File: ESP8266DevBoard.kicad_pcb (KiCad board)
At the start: 2 copper layers, 105 x 60 mm, 60 parts, among them J1 10118192-0001LF, J2 RJ11-CHINA, J3 RJ11-CHINA, J4 AC, Q1 BC847BLT1G, Q2 BC847BLT1G, Q3 2N7002H6327XTSA2, Q4 2N7002H6327XTSA2, Q5 2N7002H6327XTSA2, Q6 2N7002H6327XTSA2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

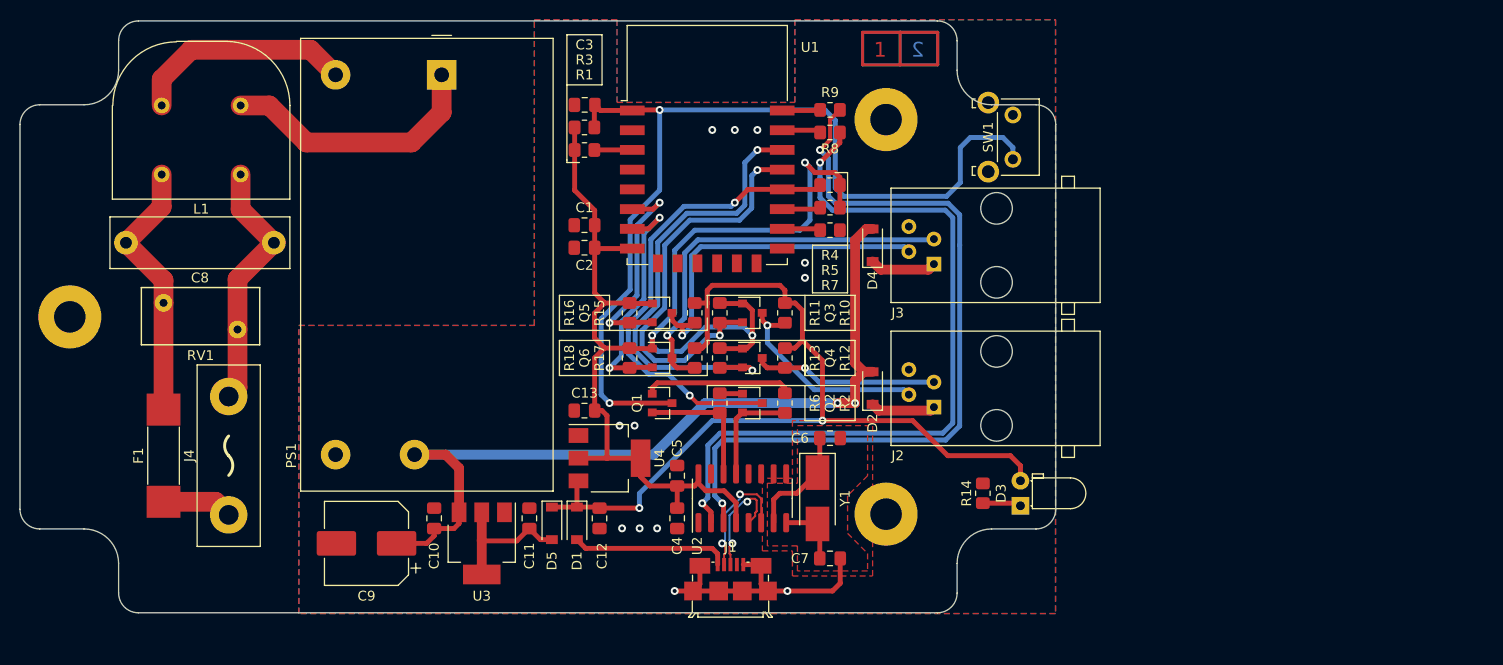
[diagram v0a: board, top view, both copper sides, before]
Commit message: RJ connectors changed, LED and buzzer controll lines added for each conector, readme file with rev changes added.
Signed-off-by: Ion Bold <bold.ion86@gmail.com>
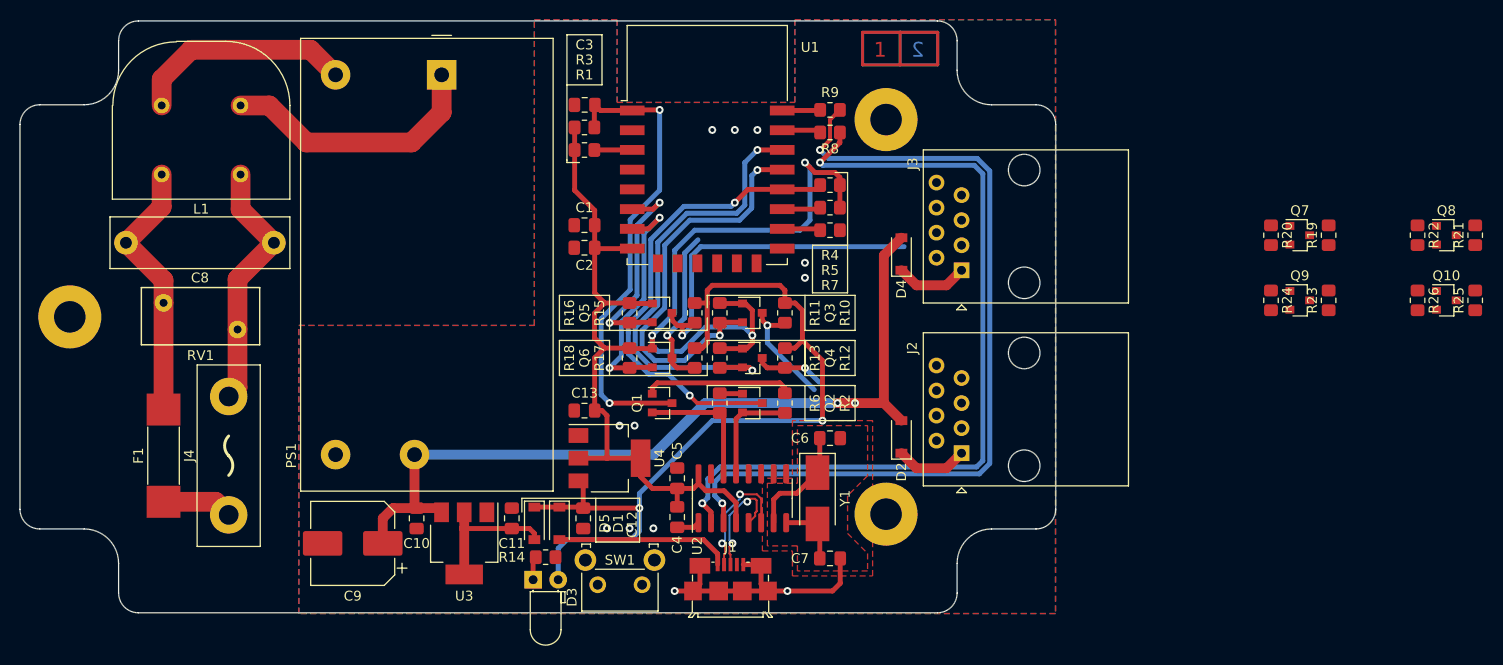
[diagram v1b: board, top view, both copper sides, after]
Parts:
- added Q10: 2N7002H6327XTSA2, Package_TO_SOT_SMD:SOT-23, F.Cu at (244.6, 68.3)
- added Q7: 2N7002H6327XTSA2, Package_TO_SOT_SMD:SOT-23, F.Cu at (229.7, 61.7)
- added Q8: 2N7002H6327XTSA2, Package_TO_SOT_SMD:SOT-23, F.Cu at (244.6, 61.7)
- added Q9: 2N7002H6327XTSA2, Package_TO_SOT_SMD:SOT-23, F.Cu at (229.7, 68.3)
- added R19: 10k, Resistor_SMD:R_0805_2012Metric_Pad1.20x1.40mm_HandSolder, F.Cu at (232.7, 61.7)
- added R20: 10k, Resistor_SMD:R_0805_2012Metric_Pad1.20x1.40mm_HandSolder, F.Cu at (226.8, 61.7)
- added R21: 10k, Resistor_SMD:R_0805_2012Metric_Pad1.20x1.40mm_HandSolder, F.Cu at (247.5, 61.7)
- added R22: 10k, Resistor_SMD:R_0805_2012Metric_Pad1.20x1.40mm_HandSolder, F.Cu at (241.7, 61.7)
- added R23: 10k, Resistor_SMD:R_0805_2012Metric_Pad1.20x1.40mm_HandSolder, F.Cu at (232.7, 68.3)
- added R24: 10k, Resistor_SMD:R_0805_2012Metric_Pad1.20x1.40mm_HandSolder, F.Cu at (226.8, 68.3)
- added R25: 10k, Resistor_SMD:R_0805_2012Metric_Pad1.20x1.40mm_HandSolder, F.Cu at (247.5, 68.3)
- added R26: 10k, Resistor_SMD:R_0805_2012Metric_Pad1.20x1.40mm_HandSolder, F.Cu at (241.7, 68.3)
- J2, J3: value RJ11-CHINA -> MTJ-881X1; footprint KiCadCustom:RJ11_6P4C-2_54mm_Horizontal -> KiCadCustom:RJ45_Multicomp_MTJ-881X1_Horizontal
- moved SW1 60.7 mm to (163.1, 97.2), turned to 180 degrees
- moved D3 50.0 mm to (152.0, 96.6), turned to 0 degrees
- moved R14 44.8 mm to (153.3, 94.4), turned to 0 degrees
- moved J2 7.47 mm to (195.5, 83.8)
- moved D2 5.75 mm to (189.4, 82.2)
- moved J3 4.36 mm to (195.5, 65.3)
- moved D4 3.05 mm to (189.4, 63.6)
- moved D5 1.78 mm to (152.1, 90.9)
- moved U3 1.78 mm to (145.0, 93.0)
- moved C10 1.78 mm to (140.2, 90.4), turned to 270 degrees
- moved C11 1.78 mm to (149.9, 90.4)
- moved D1 1.78 mm to (154.7, 90.9)
- moved C12 1.65 mm to (157.1, 90.4)
- moved C9 1.40 mm to (133.7, 93.0)
- moved C5 0.25 mm to (166.6, 86.4)
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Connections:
- J2 pad 4: GND -> Net-(J2-Pad4)
- J3 pad 4: GND -> Net-(J3-Pad4)
- U1 pad 11: Net-(U1-Pad11) -> LED_2
- U1 pad 12: Net-(U1-Pad12) -> BUZZ_2
- U1 pad 4: Net-(U1-Pad4) -> BUZZ_1
- U1 pad 5: Net-(U1-Pad5) -> LED_1
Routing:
- net RST: track 97.6 -> 48.0 mm
- net Net-(J3-Pad3): track 40.4 -> 16.5 mm
- net Net-(J2-Pad3): track 18.8 -> 7.07 mm
- net Net-(J2-Pad2): track 21.7 -> 11.9 mm
- net +5V: track 92.1 -> 85.1 mm
- net Net-(R8-Pad1): track 76.8 -> 83.6 mm
- net Net-(R9-Pad1): track 79.1 -> 85.8 mm
- net GND: track 27.2 -> 29.5 mm
- net Net-(D1-Pad2): track 16.0 -> 17.7 mm
- net Net-(D3-Pad1): track 3.92 -> 2.40 mm
- net +12V: track 87.3 -> 86.1 mm
- net Net-(D2-Pad1): track 6.62 -> 7.36 mm
- net Net-(J3-Pad2): track 35.5 -> 34.8 mm
- net Net-(D4-Pad1): track 6.79 -> 7.36 mm

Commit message: Routing done, gerber files added (v1.1).
Signed-off-by: Ion Bold <bold.ion86@gmail.com>
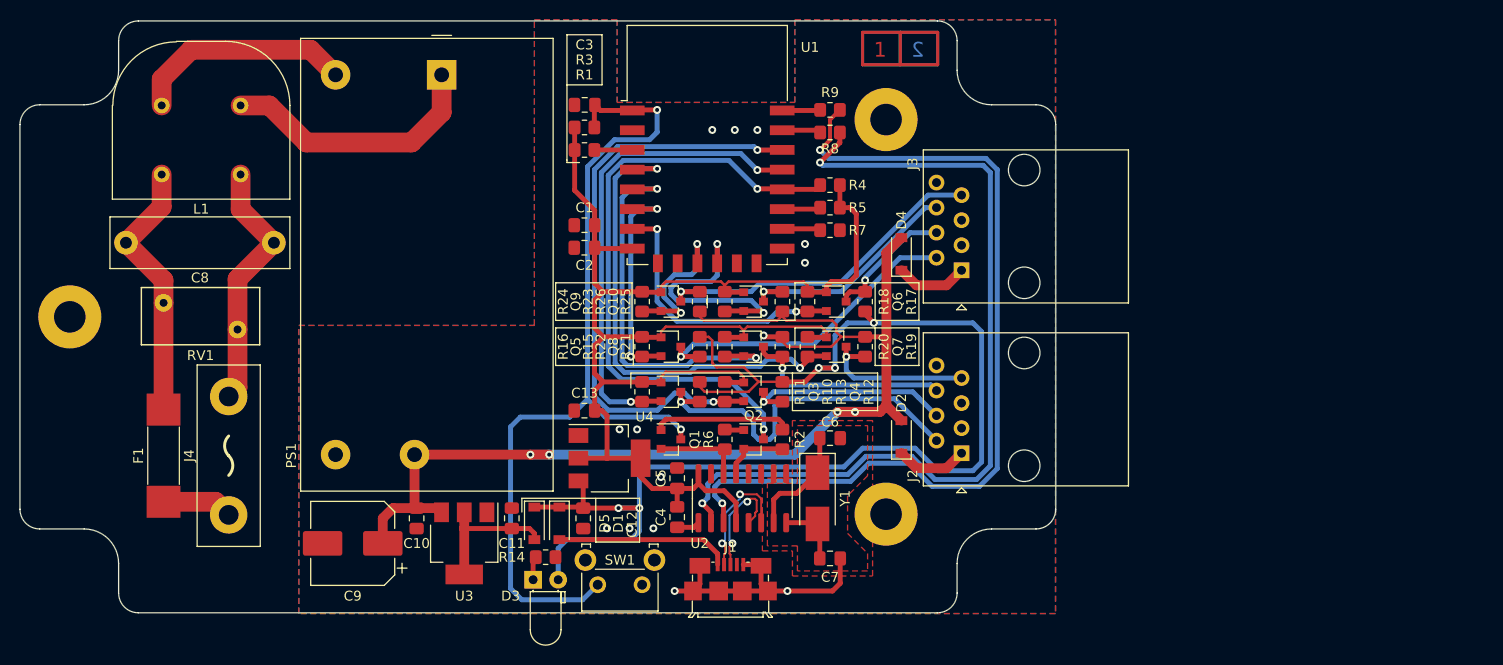
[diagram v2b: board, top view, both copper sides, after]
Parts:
- moved R22 71.1 mm to (171.4, 73.0)
- moved Q8 71.1 mm to (174.4, 73.0)
- moved R21 71.1 mm to (177.3, 73.0), turned to 270 degrees
- moved R26 70.2 mm to (171.4, 68.5)
- moved Q10 70.2 mm to (174.4, 68.5)
- moved R25 70.2 mm to (177.3, 68.5)
- moved Q9 63.8 mm to (166.0, 68.5)
- moved R23 63.8 mm to (168.9, 68.5)
- moved R24 63.8 mm to (163.1, 68.5)
- moved Q7 48.3 mm to (182.8, 73.0)
- moved R20 48.3 mm to (179.8, 73.0)
- moved R19 48.3 mm to (185.7, 73.0), turned to 270 degrees
- moved R18 18.9 mm to (179.8, 68.5)
- moved Q6 18.6 mm to (182.8, 68.5)
- moved R17 18.2 mm to (185.7, 68.5), turned to 90 degrees
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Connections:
- Q10 pad 2: LED_2 -> BUZZ_2
- Q10 pad 3: Net-(J3-Pad4) -> Net-(J3-Pad6)
- Q4 pad 3: Net-(J2-Pad3) -> Net-(J2-Pad4)
- Q6 pad 3: Net-(J3-Pad3) -> Net-(J3-Pad4)
- Q7 pad 2: BUZZ_1 -> LED_1
- Q7 pad 3: Net-(J2-Pad5) -> Net-(J2-Pad7)
- Q8 pad 2: LED_1 -> BUZZ_1
- Q8 pad 3: Net-(J2-Pad4) -> Net-(J2-Pad6)
- Q9 pad 2: BUZZ_2 -> LED_2
- Q9 pad 3: Net-(J3-Pad5) -> Net-(J3-Pad7)
- R12 pad 2: Net-(J2-Pad3) -> Net-(J2-Pad4)
- R17 pad 2: Net-(J3-Pad3) -> Net-(J3-Pad4)
- R19 pad 2: Net-(J2-Pad5) -> Net-(J2-Pad7)
- R20 pad 2: BUZZ_1 -> LED_1
- R21 pad 2: Net-(J2-Pad4) -> Net-(J2-Pad6)
- R22 pad 2: LED_1 -> BUZZ_1
- R23 pad 2: Net-(J3-Pad5) -> Net-(J3-Pad7)
- R24 pad 2: BUZZ_2 -> LED_2
- R25 pad 2: Net-(J3-Pad4) -> Net-(J3-Pad6)
- R26 pad 2: LED_2 -> BUZZ_2
- U1 pad 4: BUZZ_1 -> LED_1
- U1 pad 5: LED_1 -> BUZZ_1
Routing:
- net LED_1: track 0.00 -> 49.4 mm, vias 0 -> 2
- net +5V: track 85.1 -> 130.9 mm, vias 2 -> 5
- net RST: track 48.0 -> 90.3 mm
- net BUZZ_1: track 0.00 -> 40.4 mm, vias 0 -> 2
- net Net-(J3-Pad7): track 0.00 -> 35.4 mm, vias 0 -> 1
- net +12V: track 86.1 -> 119.3 mm, vias 2 -> 5
- net BUZZ_2: track 0.00 -> 25.2 mm, vias 0 -> 2
- net Net-(J2-Pad2): track 11.9 -> 36.3 mm
- net Net-(J3-Pad6): track 0.00 -> 24.0 mm, vias 0 -> 1
- net Net-(J2-Pad4): track 0.00 -> 21.9 mm, vias 0 -> 1
- net Net-(J2-Pad6): track 0.00 -> 21.0 mm, vias 0 -> 1
- net +3V3: track 137.2 -> 154.2 mm, vias 3 -> 0
- net Net-(J3-Pad3): track 16.5 -> 0.00 mm, vias 1 -> 0
- net Net-(J2-Pad7): track 0.00 -> 16.3 mm, vias 0 -> 1
- net LED_2: track 0.00 -> 16.2 mm, vias 0 -> 2
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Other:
- board text added: "Rev: 1.1"

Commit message: Programming connector added, gerber files generated (v1.2).
Signed-off-by: Ion Bold <bold.ion86@gmail.com>
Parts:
- added J5: 68001-420HLF, Connector_PinHeader_2.54mm:PinHeader_1x05_P2.54mm_Vertical, F.Cu at (191.8, 97.8)
- C4: value 100n -> 100n, DNP
- C5: value 10u -> 10u, DNP
- C6, C7: value 18p -> 18p, DNP
- C8: value 0.1u/275Vac -> R46KI310000M1K1
- C9: value 220u -> 865080349013
- D1: value 1N5819HWQ-7-F -> 1N5819HWQ-7-F, DNP
- J1: value 10118192-0001LF -> 10118192-0001LF, DNP
- U2: value CH340G -> CH340G, DNP
- Y1: value ABM3-12.000MHZ-D2Y-T -> ABM3-12.000MHZ-D2Y-T, DNP
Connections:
- net Net-(R8-Pad1) renamed TX
- net Net-(R9-Pad1) renamed RX
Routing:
- net RTS: track 9.03 -> 41.8 mm, vias 0 -> 1
- net DTR: track 6.81 -> 36.0 mm
- net TX: track 87.2 -> 112.7 mm
- net RX: track 89.4 -> 102.2 mm
- net GND: track 29.5 -> 26.0 mm
- net +12V: track 119.3 -> 117.4 mm
- net +3V3: track 154.2 -> 156.0 mm
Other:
- board text added: "Rev: 1.2"
- board text removed: "Rev: 1.1"

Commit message: DNP components removed from paste file, programming connector silk added, paste and silk gerbers regenerated, new ibom file generated.
Signed-off-by: Ion Bold <bold.ion86@gmail.com>
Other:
- board text added: "DTR"
- board text added: "GND"
- board text added: "RTS"
- board text added: "RX"
- board text added: "TX"
